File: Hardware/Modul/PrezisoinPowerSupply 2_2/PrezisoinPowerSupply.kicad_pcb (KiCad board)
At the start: 4 copper layers, 91 x 100 mm, 208 parts, among them J1 Supply, J2 Conn_01x03_Pin, J3 Conn_02x05_Odd_Even, J4 LEDs, J5 Sense, J6 Output, K1 EE2-5NU, Q1 IRFP240, Q2 IRFP9240, Q4 IRFP9240, Q5 MMBT3904, Q6 MMBT3904, Q7 MMBT3904, Q8 MMBT3904, Q9 IRFP240, U1 AP63200WU, U10 OPA4189, U11 OPA4189, U12 OPA189, U13 TME-1212S, U14 LM7805_TO220, U16 ATtiny3227-M, U18 LM7812_TO220, U19 TLV9301xDBV, U2 DG469, U20 ICM7555xB, U21 ADS1219, U3 ADA4522, U4 CPC1017N, U5 ISO7763FDBQ, U7 DAC8564C/D, U8 MCP9700Ax-ETT, U9 MCP9700Ax-ETT

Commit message: improove gnd
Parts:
- removed D9: SS10PH10, Package_TO_SOT_SMD:TO-277A
- added NT4: Tie, NetTie:NetTie-2_SMD_Pad2.0mm, F.Cu at (100.7, 76.5)
- moved J6 56.6 mm to (100.5, 124.1), turned to -90 degrees
- moved F2 53.1 mm to (101.0, 96.7), turned to -90 degrees
- moved C3 49.9 mm to (109.9, 141.3)
- moved R15 49.6 mm to (110.7, 133.4)
- moved R51 40.5 mm to (100.6, 136.6), turned to -90 degrees
- moved D8 32.0 mm to (107.7, 126.3)
- moved J3 31.0 mm to (134.2, 157.8), turned to -90 degrees
- moved TP28 20.8 mm to (185.1, 59.7)
- moved REF** 20.6 mm to (100.5, 145.6)
- moved C47 13.7 mm to (116.3, 161.8)
- moved U5 13.5 mm to (110.6, 158.2)
- moved TP3 7.08 mm to (178.0, 64.1)
- moved J1 5.60 mm to (100.6, 91.9)
- moved F1 4.90 mm to (101.0, 82.1)
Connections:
- Q2 pad 2: GND -> GNDPWR
- Q4 pad 2: GND -> GNDPWR
- R51 pad 4: GND -> GNDPWR
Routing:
- net /outHi: track 187.6 -> 165.4 mm, vias 25 -> 17
- net Net-(J6-Pin_1): track 14.0 -> 0.00 mm
- net Tx: track 14.9 -> 1.25 mm
- net ISOTx: track 13.5 -> 0.00 mm
- net +5V: track 224.3 -> 210.9 mm
- net DataOut1: track 12.9 -> 0.00 mm
- net DataOut2: track 12.3 -> 0.00 mm
- net ISO DataIn1: track 12.1 -> 0.00 mm
- net Rx: track 11.5 -> 0.16 mm, vias 2 -> 0
- net DataIn1: track 10.4 -> 0.00 mm
- net ISORx: track 10.3 -> 0.00 mm
- net DataIn2: track 9.92 -> 0.00 mm
- net ISO DataIn2: track 9.27 -> 0.00 mm
- net ISO DataOut2: track 8.90 -> 0.00 mm
- net /outLOW: track 7.79 -> 0.00 mm
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- removed copper zone on F.Cu, net GND1
- removed copper zone on In1.Cu, net GND1
- removed copper zone on In2.Cu, net GND1
- removed copper zone on B.Cu, net VCCQ

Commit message: work hardware
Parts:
- removed C5: 1u, Capacitor_SMD:C_0603_1608Metric
- removed C56: 100u, Capacitor_SMD:CP_Elec_8x10.5
- added C18: 10u, Capacitor_SMD:C_1206_3216Metric, F.Cu at (160.4, 64.5)
- added C19: 100n, Capacitor_SMD:C_0603_1608Metric, F.Cu at (116.5, 136.1)
- added C39: 100n, Capacitor_SMD:C_0603_1608Metric, F.Cu at (116.5, 139.2)
- added D9: 1N4148WS, Diode_SMD:D_SOD-323, F.Cu at (136.2, 162.4)
- added J7: USB_C_Receptacle, Connector_USB:USB_C_Receptacle_GCT_USB4115-03-C, F.Cu at (113.8, 144.8)
- added NT2: Tie, NetTie:NetTie-2_SMD_Pad2.0mm, F.Cu at (107.4, 89.0)
- added R37: 5,1k, Resistor_SMD:R_0603_1608Metric, F.Cu at (115.4, 149.1)
- added R47: 5,1k, Resistor_SMD:R_0603_1608Metric, F.Cu at (113.8, 140.7)
- added U6: CH340C, Package_SO:SOIC-16_3.9x9.9mm_P1.27mm, F.Cu at (122.5, 136.6)
- U13: moved to B.Cu
- moved FB1 72.8 mm to (185.2, 165.6)
- moved FB2 72.8 mm to (192.8, 165.3)
- moved FB3 72.8 mm to (196.7, 165.3)
- moved R14 72.8 mm to (193.2, 174.2)
- moved R35 72.8 mm to (193.2, 172.6)
- moved C40 72.8 mm to (186.3, 166.8)
- moved TP12 72.8 mm to (180.6, 171.1)
- moved U16 72.8 mm to (188.9, 169.2)
- moved U5 59.2 mm to (168.2, 172.0)
- moved C47 59.2 mm to (173.9, 175.6)
- moved C46 46.1 mm to (159.8, 168.4)
- moved TP29 42.2 mm to (133.1, 66.6)
- moved J2 41.0 mm to (155.5, 133.9)
- moved C15 40.9 mm to (182.4, 66.7), turned to 90 degrees
- moved C16 39.1 mm to (179.3, 66.6), turned to 90 degrees
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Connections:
- C3 pad 1: GND -> GNDPWR
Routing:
- net GNDPWR: track 0.00 -> 151.7 mm
- net +5V: track 210.9 -> 132.9 mm, vias 5 -> 3
- net +12V: track 122.2 -> 92.8 mm
- net TempData#1: track 40.5 -> 12.7 mm
- net Net-(R41-Pad2): track 23.6 -> 0.00 mm
- net /buckConLDO/-12V: track 22.3 -> 0.00 mm
- net Net-(R39-Pad2): track 21.8 -> 0.00 mm
- net +VDC: track 162.8 -> 143.6 mm
- net Net-(U6-UD-): track 0.00 -> 16.9 mm, vias 0 -> 2
- net /buckConLDO/..36V: track 19.0 -> 2.54 mm
- net Net-(U6-UD+): track 0.00 -> 14.7 mm
- net +36V: track 19.7 -> 7.43 mm, vias 3 -> 2
- net UPDI: track 13.5 -> 2.75 mm, vias 1 -> 0
- net DAC Reset: track 19.8 -> 9.31 mm
- net /outHi: track 165.4 -> 175.6 mm, vias 17 -> 26
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- added copper zone on F.Cu, net GNDPWR
- removed copper zone on B.Cu, net GND
- removed copper zone on In1.Cu, net GND

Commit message: hardware
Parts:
- moved R37 71.9 mm to (185.0, 131.2), turned to 180 degrees
- moved J7 68.6 mm to (181.9, 137.2), turned to -90 degrees
- moved R47 64.8 mm to (178.4, 145.8), turned to -90 degrees
- moved C39 59.9 mm to (176.1, 144.9), turned to 0 degrees
- moved C19 57.3 mm to (173.0, 144.9), turned to 0 degrees
- moved U6 52.2 mm to (174.7, 138.9), turned to 180 degrees
- moved J3 31.7 mm to (136.0, 141.4), turned to 0 degrees
- moved TP26 14.6 mm to (179.6, 125.3)
- moved C30 4.23 mm to (178.8, 129.8), turned to 90 degrees
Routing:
- net +5V: track 132.9 -> 113.4 mm, vias 3 -> 2
- net Net-(U6-UD-): track 16.9 -> 7.73 mm
- net Net-(U6-UD+): track 14.7 -> 6.98 mm
- net Net-(J7-CC2): track 3.29 -> 8.86 mm
- net Net-(J7-CC1): track 3.53 -> 8.52 mm
- net /buckConLDO/Vout 5V: track 17.0 -> 15.6 mm
- net GND: vias 169 -> 161

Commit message: hardware work
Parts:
- removed D9: 1N4148WS, Diode_SMD:D_SOD-323
- added C5: 1u, Capacitor_SMD:C_0603_1608Metric, F.Cu at (131.8, 131.2)
- added R52: 5,1k, Resistor_SMD:R_0603_1608Metric, F.Cu at (168.9, 139.6)
- moved U16 51.1 mm to (149.3, 136.9), turned to -135 degrees
- moved C40 47.4 mm to (151.7, 134.3), turned to -45 degrees
- moved FB1 45.8 mm to (152.9, 133.2), turned to 135 degrees
- moved J3 29.6 mm to (112.5, 159.5), turned to 90 degrees
- moved TP12 25.3 mm to (156.9, 162.2)
- moved R47 9.71 mm to (186.1, 139.7)
- moved J2 9.16 mm to (164.7, 133.5)
- moved R37 4.62 mm to (186.1, 135.7), turned to 90 degrees
- moved C39 1.58 mm to (177.7, 145.0), turned to 180 degrees
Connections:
- C19 pad 1: +5V -> RESET
- C35 pad 1: +5V -> RESET
- C43 pad 1: +5V -> RESET
- C44 pad 1: +5V -> RESET
- C46 pad 1: +5V -> RESET
- D2 pad 1: +5V -> RESET
- FB1 pad 1: +5V -> RESET
- FB2 pad 1: +5V -> RESET
- FB3 pad 1: +5V -> RESET
- FB4 pad 1: +5V -> RESET
- FB5 pad 2: +5V -> RESET
- J2 pad 1: +5V -> RESET
- J4 pad 2: +5V -> RESET
- JP1 pad 2: +5V -> RESET
- K1 pad 1: +5V -> RESET
- R14 pad 2: +5V -> RESET
- R35 pad 2: +5V -> RESET
- U16 pad 22: RESET -> unconnected-(U16-PC5-Pad22)
- U16 pad 7: DAC Reset -> unconnected-(U16-PA6-Pad7)
- U5 pad 1: +5V -> RESET
- U6 pad 16: +5V -> RESET
- U6 pad 2: unconnected-(U6-TXD-Pad2) -> Net-(U6-TXD)
- U6 pad 3: unconnected-(U6-RXD-Pad3) -> UPDI
- U7 pad 13: DAC Reset -> GND
- U8 pad 1: +5V -> RESET
- U9 pad 1: +5V -> RESET
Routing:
- net +5V: track 113.4 -> 0.00 mm, vias 2 -> 0
- net RESET: track 17.3 -> 92.1 mm, vias 2 -> 1
- net ON: track 56.9 -> 28.9 mm, vias 3 -> 2
- net TempData#2: track 86.9 -> 61.9 mm
- net DRDY: track 17.3 -> 3.97 mm, vias 2 -> 1
- net SDA: track 14.9 -> 2.99 mm, vias 2 -> 1
- net DAC Sync: track 15.4 -> 4.30 mm
- net SCL: track 19.7 -> 8.65 mm, vias 2 -> 1
- net DAC Reset: track 9.31 -> 0.00 mm
- net SensSW: track 58.8 -> 50.2 mm
- net ON PhotoMos: track 66.6 -> 58.3 mm, vias 2 -> 1
- net TempData#1: track 12.7 -> 4.49 mm, vias 1 -> 0
- net DAC Enable: track 8.04 -> 0.00 mm
- net DAC LDAC: track 7.23 -> 0.00 mm
- net Net-(J7-CC1): track 8.52 -> 3.31 mm
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
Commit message: hardware work ##
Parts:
- added D9: LED, LED_SMD:LED_0603_1608Metric, F.Cu at (178.9, 122.0)
- added K2: G2RL-2, Relay_THT:Relay_SPDT_Omron_G2RL-1-E, F.Cu at (87.3, 144.2)
- added R53: 1k, Resistor_SMD:R_0603_1608Metric, F.Cu at (175.4, 122.0)
- added R54: 1k, Resistor_SMD:R_0603_1608Metric, F.Cu at (124.9, 114.1)
- moved R14 87.5 mm to (123.9, 120.7), turned to 180 degrees
- moved R35 85.7 mm to (123.9, 122.2), turned to 180 degrees
- moved FB3 73.0 mm to (131.9, 131.7)
- moved FB2 72.9 mm to (128.1, 131.7)
- moved C47 34.4 mm to (152.2, 148.8), turned to 180 degrees
- moved U5 30.2 mm to (154.6, 145.0)
- moved J3 26.0 mm to (135.0, 146.3)
- moved TP12 23.1 mm to (175.5, 148.5)
- moved C46 19.8 mm to (156.6, 148.8), turned to 180 degrees
- moved U16 11.2 mm to (160.4, 137.7), turned to -45 degrees
- moved C40 5.71 mm to (157.4, 134.7), turned to 45 degrees
- moved J2 4.47 mm to (168.1, 130.6)
- moved FB1 3.46 mm to (156.3, 133.6), turned to -135 degrees
- moved FB4 2.44 mm to (120.7, 122.7)
- moved C38 2.44 mm to (120.7, 121.1)
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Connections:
- net RESET renamed +5V
- C48 pad 1: 2,5Vref -> Net-(U21-REFP)
- U21 pad 9: 2,5Vref -> Net-(U21-REFP)
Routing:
- net TempData#1: track 4.49 -> 79.0 mm, vias 0 -> 2
- net Net-(R41-Pad2): track 0.00 -> 45.5 mm, vias 0 -> 2
- net Net-(R39-Pad2): track 0.00 -> 44.9 mm, vias 0 -> 2
- net DRDY: track 3.97 -> 46.1 mm, vias 1 -> 2
- net ON: track 28.9 -> 59.3 mm
- net TempData#2: track 61.9 -> 42.1 mm, vias 0 -> 1
- net ISO DataOut1: track 0.00 -> 18.2 mm, vias 0 -> 1
- net ISO DataOut2: track 0.00 -> 17.7 mm, vias 0 -> 1
- net ISOTx: track 0.00 -> 15.7 mm
- net ISORx: track 0.00 -> 13.7 mm
- net SensSW: track 50.2 -> 63.2 mm, vias 3 -> 2
- net ISO DataIn1: track 0.00 -> 10.8 mm, vias 0 -> 1
- net ISO DataIn2: track 0.00 -> 10.7 mm, vias 0 -> 1
- net Tx: track 0.00 -> 10.4 mm
- net ON PhotoMos: track 58.3 -> 48.4 mm, vias 1 -> 2
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- added copper zone on F.Cu, net GND1
- added copper zone on B.Cu, net VCCQ

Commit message: hardware relay
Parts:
- removed K2: G2RL-2, Relay_THT:Relay_SPDT_Omron_G2RL-1-E
- added K3: SANYOU_SRD_Form_C, Relay_THT:Relay_SPDT_SANYOU_SRD_Series_Form_C, B.Cu at (112.2, 147.9)

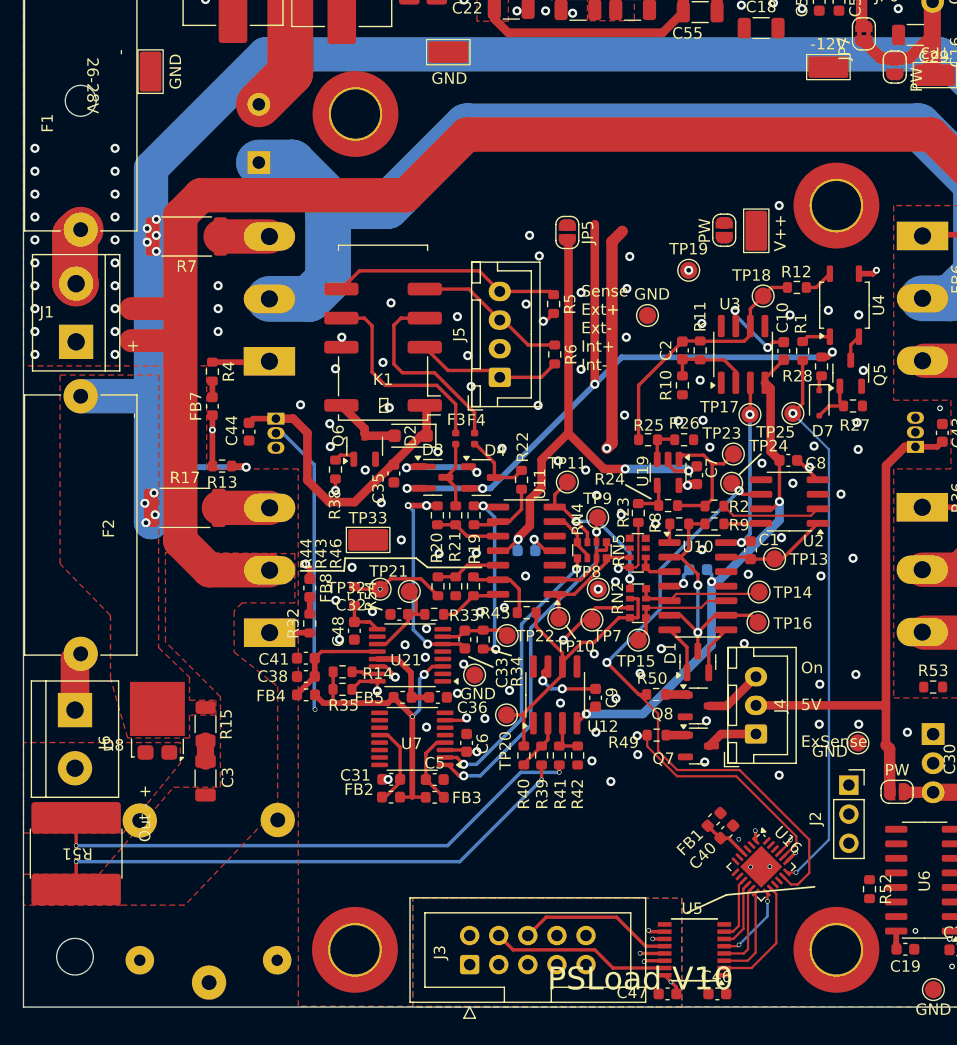
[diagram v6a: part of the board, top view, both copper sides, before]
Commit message: range switch
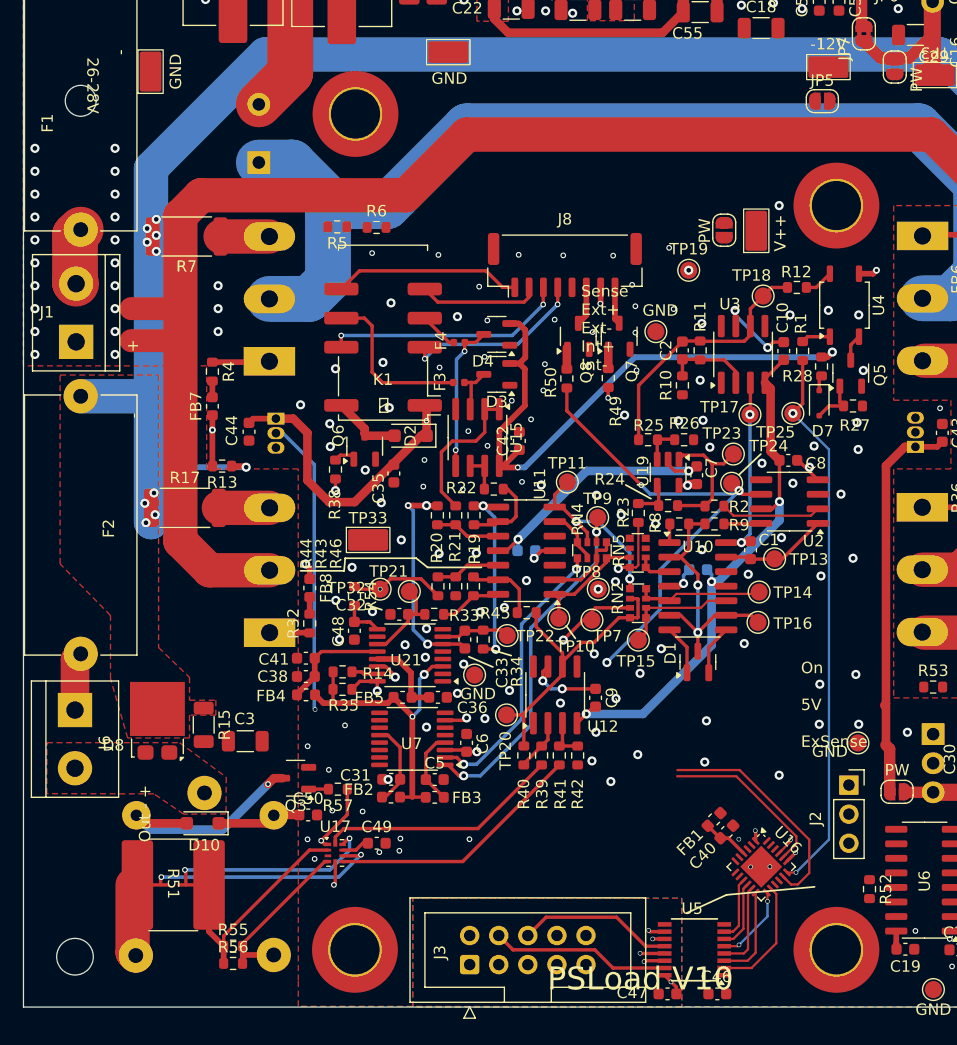
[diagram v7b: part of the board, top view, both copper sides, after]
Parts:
- removed J4: LEDs, Connector_JST:JST_XH_B3B-XH-A_1x03_P2.50mm_Vertical
- removed J5: Sense, Connector_JST:JST_XH_B4B-XH-A_1x04_P2.50mm_Vertical
- added C42: 100n, Capacitor_SMD:C_0603_1608Metric, F.Cu at (139.3, 100.6)
- added C49: 100n, Capacitor_SMD:C_0603_1608Metric, F.Cu at (126.9, 135.7)
- added C50: 100n, Capacitor_SMD:C_0603_1608Metric, F.Cu at (120.9, 133.2)
- added D10: 1N4007, Diode_SMD:D_SOD-123F, F.Cu at (111.7, 133.9)
- added J8: Conn_01x08_Socket, Connector_JST:JST_GH_BM08B-GHS-TBT_1x08-1MP_P1.25mm_Vertical, F.Cu at (143.3, 85.2)
- added Q3: MMBT3904, Package_TO_SOT_SMD:SOT-23-3, F.Cu at (119.8, 130.0)
- added R55: 10 0,05%, Resistor_SMD:R_0603_1608Metric, F.Cu at (114.3, 144.7)
- added R56: 10 0,05%, Resistor_SMD:R_0603_1608Metric, F.Cu at (114.3, 146.2)
- added R57: 1k, Resistor_SMD:R_0603_1608Metric, F.Cu at (123.5, 131.0)
- added U15: OPA2192, Package_SO:SOIC-8_3.9x4.9mm_P1.27mm, F.Cu at (135.7, 100.3)
- added U17: TS5A23159RSE, Package_DFN_QFN:Texas_R-PUQFN-N10, F.Cu at (123.2, 136.5)
- moved Q7 36.5 mm to (148.0, 91.4), turned to 90 degrees
- moved Q8 33.9 mm to (144.5, 91.4), turned to 90 degrees
- moved R49 31.5 mm to (147.1, 95.1), turned to 90 degrees
- moved R50 28.7 mm to (143.5, 95.1), turned to 90 degrees
- moved JP5 25.1 mm to (165.8, 70.9), turned to 0 degrees
- moved R5 20.1 mm to (123.4, 81.9), turned to 180 degrees
- moved R6 19.1 mm to (126.8, 81.9), turned to 0 degrees
- moved K3 16.6 mm to (111.8, 131.3), turned to -90 degrees
- moved D4 12.6 mm to (137.3, 91.2), turned to 180 degrees
- moved D3 10.6 mm to (137.3, 94.7), turned to 180 degrees
- moved R51 8.91 mm to (109.1, 139.3), turned to 0 degrees
- moved F4 8.50 mm to (134.1, 92.0), turned to 180 degrees
- moved F3 4.91 mm to (134.0, 95.5), turned to 180 degrees
- moved C3 4.73 mm to (115.4, 126.8), turned to 180 degrees
- moved R22 2.55 mm to (137.1, 104.8), turned to 180 degrees
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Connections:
- D3 pad 1: -12V -> GND
- D3 pad 3: Net-(D3-K-Pad3) -> Net-(U15A-+)
- D4 pad 1: -12V -> GND
- D4 pad 3: Net-(D4-K-Pad3) -> Net-(U15B-+)
- F3 pad 1: Net-(D3-K-Pad3) -> Net-(U15A-+)
- F4 pad 1: Net-(D4-K-Pad3) -> Net-(U15B-+)
- K3 pad 1: unconnected-(K3-Pad1) -> /outLOW
- K3 pad 2: unconnected-(K3-Pad2) -> +12V
- K3 pad 3: unconnected-(K3-Pad3) -> Net-(K3-Pad3)
- K3 pad 4: unconnected-(K3-Pad4) -> Net-(K3-Pad4)
- K3 pad 5: unconnected-(K3-Pad5) -> Net-(D10-A)
- R21 pad 2: Net-(D3-K-Pad3) -> Net-(U15A--)
- R22 pad 2: Net-(D4-K-Pad3) -> Net-(U15B--)
- R5 pad 1: /ExSense+ -> /outHi
- R5 pad 2: /IntSense+ -> Net-(F3-Pad2)
- R51 pad 1: /outLOW -> Net-(K3-Pad4)
- R51 pad 2: Net-(R41-Pad2) -> Net-(R51-Pad2)
- R51 pad 3: Net-(R39-Pad2) -> Net-(R51-Pad3)
- R6 pad 1: /ExSense- -> /outLOW
- R6 pad 2: /IntSense- -> Net-(F4-Pad2)
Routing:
- net -12V: track 126.6 -> 84.6 mm, vias 8 -> 5
- net Net-(R39-Pad2): track 44.9 -> 21.2 mm, vias 2 -> 0
- net Net-(R41-Pad2): track 45.5 -> 22.4 mm, vias 2 -> 0
- net +12V: track 92.8 -> 70.1 mm, vias 7 -> 6
- net Net-(R51-Pad2): track 0.00 -> 20.6 mm, vias 0 -> 2
- net GNDPWR: track 151.7 -> 172.2 mm
- net Net-(D10-A): track 0.00 -> 19.9 mm, vias 0 -> 1
- net SensSW: track 63.2 -> 81.6 mm
- net Net-(R51-Pad3): track 0.00 -> 18.3 mm, vias 0 -> 2
- net Net-(K3-Pad3): track 0.00 -> 14.9 mm
- net Net-(F4-Pad2): track 16.9 -> 3.41 mm
- net Net-(U15B-+): track 0.00 -> 13.1 mm, vias 0 -> 2
- net Net-(U15A--): track 0.00 -> 13.0 mm
- net RangeSW: track 0.00 -> 12.5 mm, vias 0 -> 2
- net +5V: track 101.4 -> 113.6 mm, vias 2 -> 4
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- removed copper zone on F.Cu, net GNDPWR
